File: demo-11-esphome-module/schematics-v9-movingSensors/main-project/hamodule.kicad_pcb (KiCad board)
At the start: 2 copper layers, 145.4 x 76.2 mm, 62 parts, among them J1 1017505, J2 Conn-ESP-Relays, J3 1017505, J4 Conn-Buttons, J5 Conn_01x02, J6 Conn-Esp-Sensors, J7 Conn-LedIndicators, J8 1017505, K1 G5Q-1, K2 G5Q-1, K3 G5Q-1, K4 G5Q-1, U1 ULN2003A, U2 LD1117S33TR_SOT223, U3 HCPL3700, U4 HCPL3700, U5 HCPL3700, U6 HCPL3700

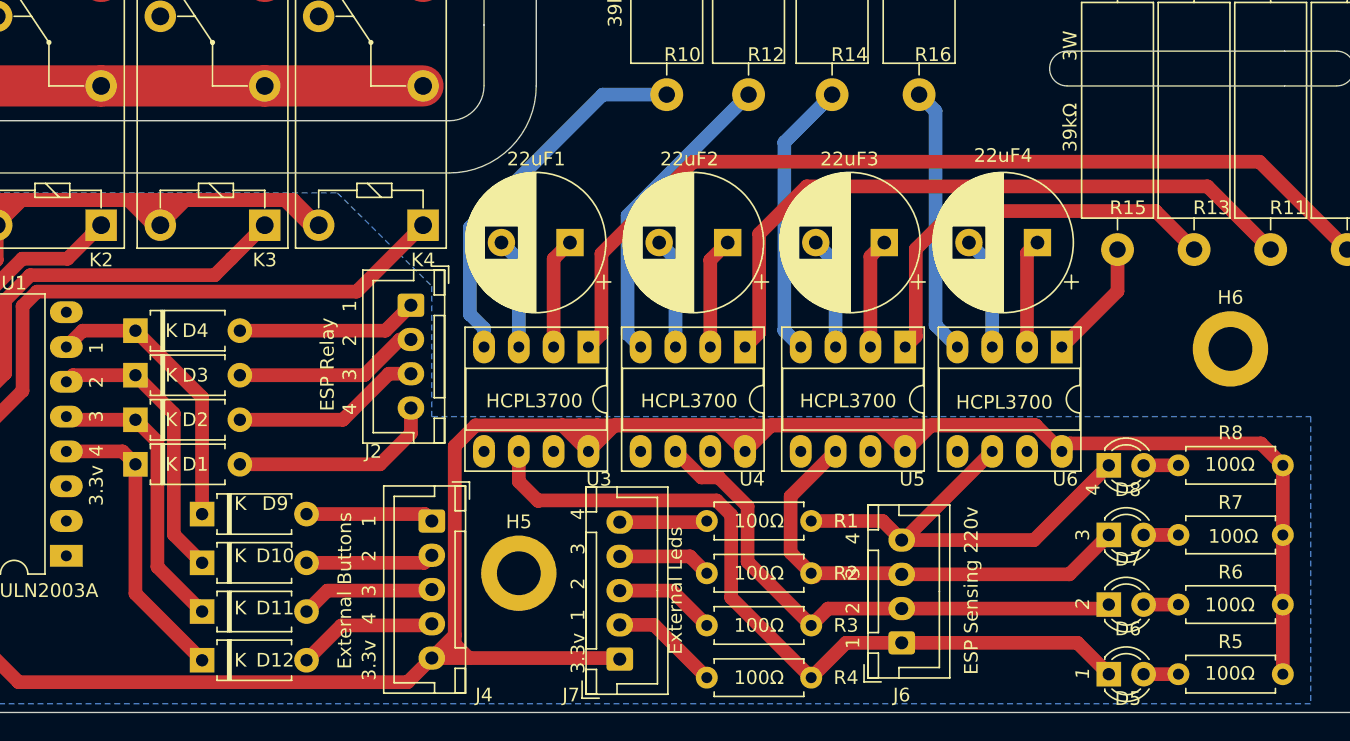
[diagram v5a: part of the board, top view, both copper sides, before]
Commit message: adding mounting holes for ESP board
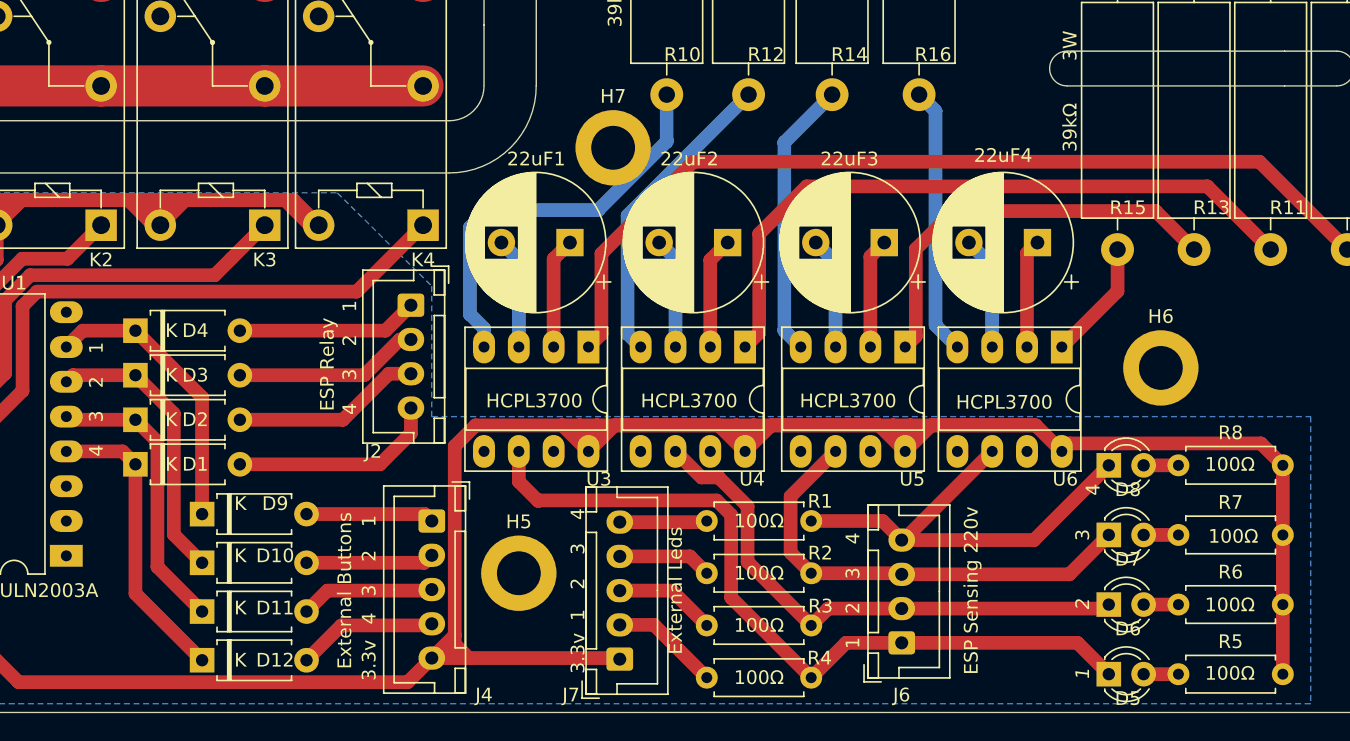
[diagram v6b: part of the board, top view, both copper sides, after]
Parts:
- added H7: MountingHole_Pad, MountingHole:MountingHole_3.2mm_M3_ISO14580_Pad, F.Cu at (109.8, 46.4)
- moved H6 5.27 mm to (149.7, 62.5)
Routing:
- net Net-(R10-Pad2): track 27.5 -> 29.5 mm
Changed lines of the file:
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@@
   (general
     (thickness 1.6)
-    (drawings 116)
-    (tracks 282)
+    (drawings 115)
+    (tracks 284)
     (zones 0)
-    (modules 62)
-    (nets 77)
+    (modules 63)
+    (nets 78)
   )
   (page A4)
   (layers
-    (0 F.Cu signal)
-    (31 B.Cu signal)
+    (0 F.Cu signal hide)
+    (31 B.Cu signal hide)
     (32 B.Adhes user hide)
     (33 F.Adhes user hide)
@@
   (net 75 "Net-(U5-Pad7)")
   (net 76 "Net-(U6-Pad7)")
+  (net 77 "Net-(H7-Pad1)")
   (net_class Default "This is the default net class."
     (clearance 0.2)
@@
     (add_net "Net-(H5-Pad1)")
     (add_net "Net-(H6-Pad1)")
+    (add_net "Net-(H7-Pad1)")
     (add_net "Net-(J3-Pad3)")
     (add_net "Net-(J3-Pad4)")
@@
     (add_net Sens4)
   )
+  (module MountingHole:MountingHole_3.2mm_M3_ISO14580_Pad (layer F.Cu)
+    (at 109.7534 46.42358)
+    (descr "Mounting Hole 3.2mm, M3, ISO14580")
+    (tags "mounting hole 3.2mm m3 iso14580")
+    (attr virtual)
+    (fp_text reference H7 (at 0 -3.75) (layer F.SilkS)
+      (effects (font (size 1 1) (thickness 0.15)))
+    )
+    (fp_text value MountingHole_Pad (at 0 3.75) (layer F.Fab)
+      (effects (font (size 1 1) (thickness 0.15)))
+    )
+    (fp_text user %R (at 0.3 0) (layer F.Fab)
+      (effects (font (size 1 1) (thickness 0.15)))
+    )
+    (fp_circle (center 0 0) (end 2.75 0) (layer Cmts.User) (width 0.15))
+    (fp_circle (center 0 0) (end 3 0) (layer F.CrtYd) (width 0.05))
+    (pad 1 thru_hole circle (at 0 0) (size 5.5 5.5) (drill 3.2) (layers *.Cu *.Mask)
+      (net 77 "Net-(H7-Pad1)"))
+  )
   (module Capacitor_THT:CP_Radial_D6.3mm_P2.50mm (layer F.Cu)
     (at 60.96 80.01 270)
@@
     (descr "Resistor, Axial_DIN0207 series, Axial, Horizontal, pin pitch=7.62mm, 0.25W = 1/4W, length*diameter=6.3*2.5mm^2, http://cdn-reichelt.de/documents/datenblatt/B400/1_4W%23YAG.pdf")
     (tags "Resistor Axial_DIN0207 series Axial Horizontal pin pitch 7.62mm 0.25W = 1/4W length 6.3mm diameter 2.5mm")
-    (fp_text reference R4 (at -2.54 0) (layer F.SilkS)
+    (fp_text reference R4 (at -0.61468 1.42494) (layer F.SilkS)
       (effects (font (size 1 1) (thickness 0.15)))
     )
@@
     (descr "Resistor, Axial_DIN0207 series, Axial, Horizontal, pin pitch=7.62mm, 0.25W = 1/4W, length*diameter=6.3*2.5mm^2, http://cdn-reichelt.de/documents/datenblatt/B400/1_4W%23YAG.pdf")
     (tags "Resistor Axial_DIN0207 series Axial Horizontal pin pitch 7.62mm 0.25W = 1/4W length 6.3mm diameter 2.5mm")
-    (fp_text reference R3 (at -2.54 0) (layer F.SilkS)
+    (fp_text reference R3 (at -0.68326 1.41224) (layer F.SilkS)
       (effects (font (size 1 1) (thickness 0.15)))
     )
@@
     (descr "Resistor, Axial_DIN0207 series, Axial, Horizontal, pin pitch=7.62mm, 0.25W = 1/4W, length*diameter=6.3*2.5mm^2, http://cdn-reichelt.de/documents/datenblatt/B400/1_4W%23YAG.pdf")
     (tags "Resistor Axial_DIN0207 series Axial Horizontal pin pitch 7.62mm 0.25W = 1/4W length 6.3mm diameter 2.5mm")
-    (fp_text reference R2 (at -2.54 0) (layer F.SilkS)
+    (fp_text reference R2 (at -0.66548 1.46812) (layer F.SilkS)
       (effects (font (size 1 1) (thickness 0.15)))
     )
@@
     (descr "Resistor, Axial_DIN0207 series, Axial, Horizontal, pin pitch=7.62mm, 0.25W = 1/4W, length*diameter=6.3*2.5mm^2, http://cdn-reichelt.de/documents/datenblatt/B400/1_4W%23YAG.pdf")
     (tags "Resistor Axial_DIN0207 series Axial Horizontal pin pitch 7.62mm 0.25W = 1/4W length 6.3mm diameter 2.5mm")
-    (fp_text reference R1 (at -2.54 0) (layer F.SilkS)
+    (fp_text reference R1 (at -0.6477 1.43764) (layer F.SilkS)
       (effects (font (size 1 1) (thickness 0.15)))
     )
@@
   )
   (module MountingHole:MountingHole_3.2mm_M3_ISO14580_Pad (layer F.Cu)
-    (at 154.8 61.1)
+    (at 149.7203 62.48908)
     (descr "Mounting Hole 3.2mm, M3, ISO14580")
     (tags "mounting hole 3.2mm m3 iso14580")
@@
     (effects (font (size 1 1) (thickness 0.15)))
   )
-  (gr_text 3.3v (at 72.044 71.07 90) (layer F.SilkS)
-    (effects (font (size 1 1) (thickness 0.15)))
-  )
   (gr_text 4 (at 91.974 31.794) (layer F.SilkS)
     (effects (font (size 1 1) (thickness 0.15) italic))
@@
   (segment (start 44.45 27.94) (end 44.45 30.48) (width 3) (layer F.Cu) (net 26))
   (segment (start 44.45 33.655) (end 44.45 27.94) (width 3) (layer F.Cu) (net 26))
-  (segment (start 99.299999 52.235999) (end 108.990998 42.545) (width 1) (layer B.Cu) (net 27))
-  (segment (start 99.299999 58.576179) (end 99.299999 52.235999) (width 1) (layer B.Cu) (net 27))
-  (segment (start 108.990998 42.545) (end 113.665 42.545) (width 1) (layer B.Cu) (net 27))
-  (segment (start 100.33 59.60618) (end 99.299999 58.576179) (width 1) (layer B.Cu) (net 27))
-  (segment (start 100.33 60.96) (end 100.33 59.60618) (width 1) (layer B.Cu) (net 27))
+  (segment (start 100.33 59.60618) (end 100.33 60.96) (width 1) (layer B.Cu) (net 27))
+  (segment (start 99.299999 58.576179) (end 100.33 59.60618) (width 1) (layer B.Cu) (net 27))
+  (segment (start 113.665 42.545) (end 113.665 45.968402) (width 1) (layer B.Cu) (net 27))
+  (segment (start 113.665 45.968402) (end 108.660682 50.97272) (width 1) (layer B.Cu) (net 27))
+  (segment (start 108.660682 50.97272) (end 100.563278 50.97272) (width 1) (layer B.Cu) (net 27))
+  (segment (start 100.563278 50.97272) (end 99.299999 52.235999) (width 1) (layer B.Cu) (net 27))
+  (segment (start 99.299999 52.235999) (end 99.299999 58.576179) (width 1) (layer B.Cu) (net 27))
   (segment (start 140.469 75.05) (end 145.923 69.596) (width 1) (layer F.Cu) (net 28))
   (segment (start 130.81 75.05) (end 140.469 75.05) (width 1) (layer F.Cu) (net 28))

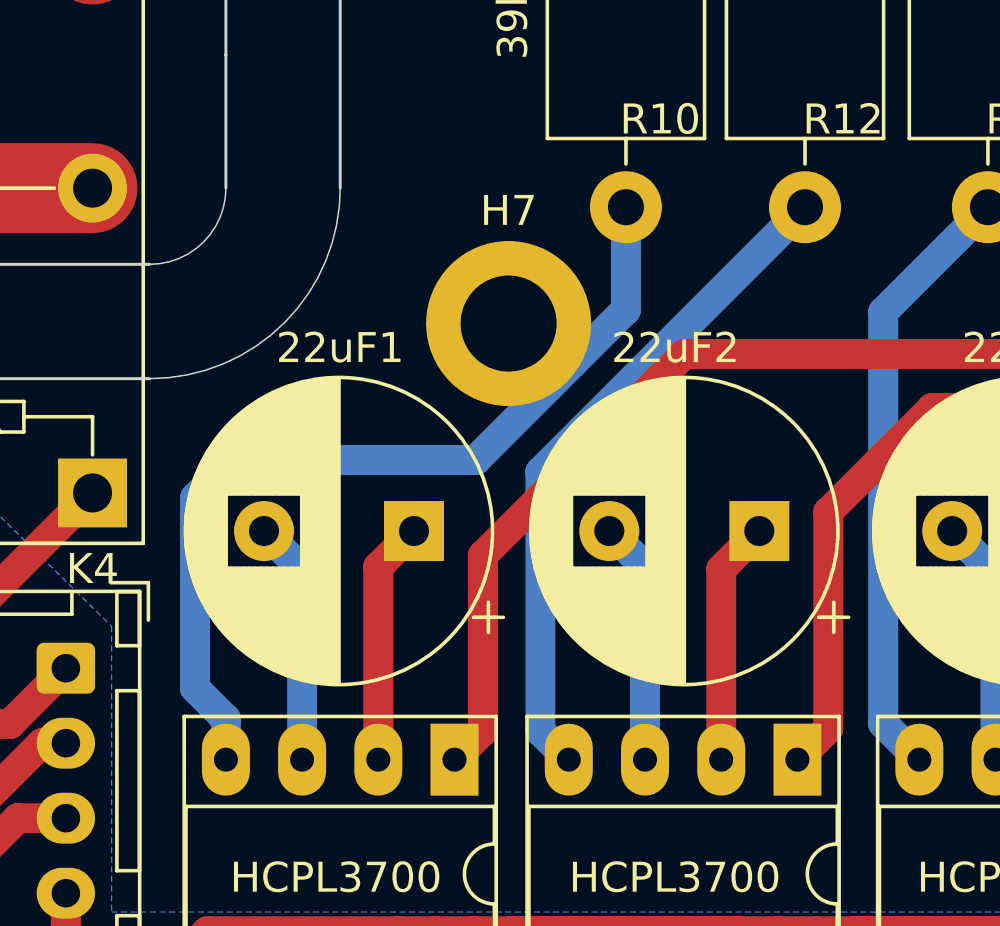
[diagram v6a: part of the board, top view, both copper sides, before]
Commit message: mounting holes + text correction + ...
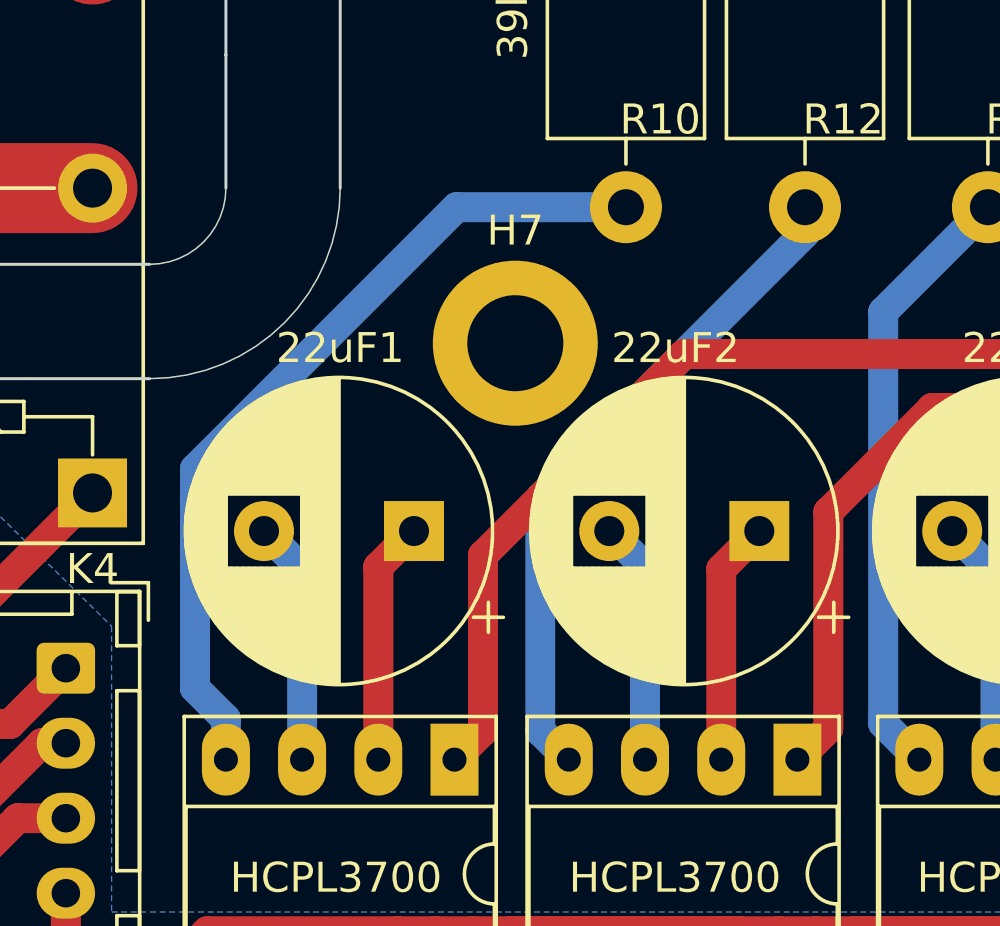
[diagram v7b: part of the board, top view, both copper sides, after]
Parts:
- moved H7 0.69 mm to (110.0, 47.1)
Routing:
- net Net-(R10-Pad2): track 29.5 -> 28.1 mm
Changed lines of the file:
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@@
     (thickness 1.6)
     (drawings 115)
-    (tracks 284)
+    (tracks 283)
     (zones 0)
     (modules 63)
@@
   (page A4)
   (layers
-    (0 F.Cu signal hide)
+    (0 F.Cu signal)
     (31 B.Cu signal hide)
     (32 B.Adhes user hide)
@@
   )
   (module MountingHole:MountingHole_3.2mm_M3_ISO14580_Pad (layer F.Cu)
-    (at 109.7534 46.42358)
+    (at 109.97692 47.0789)
     (descr "Mounting Hole 3.2mm, M3, ISO14580")
     (tags "mounting hole 3.2mm m3 iso14580")
@@
   (segment (start 100.33 59.60618) (end 100.33 60.96) (width 1) (layer B.Cu) (net 27))
   (segment (start 99.299999 58.576179) (end 100.33 59.60618) (width 1) (layer B.Cu) (net 27))
-  (segment (start 113.665 42.545) (end 113.665 45.968402) (width 1) (layer B.Cu) (net 27))
-  (segment (start 113.665 45.968402) (end 108.660682 50.97272) (width 1) (layer B.Cu) (net 27))
-  (segment (start 108.660682 50.97272) (end 100.563278 50.97272) (width 1) (layer B.Cu) (net 27))
-  (segment (start 100.563278 50.97272) (end 99.299999 52.235999) (width 1) (layer B.Cu) (net 27))
-  (segment (start 99.299999 52.235999) (end 99.299999 58.576179) (width 1) (layer B.Cu) (net 27))
+  (segment (start 99.299999 51.264549) (end 99.299999 58.576179) (width 1) (layer B.Cu) (net 27))
+  (segment (start 108.019548 42.545) (end 99.299999 51.264549) (width 1) (layer B.Cu) (net 27))
+  (segment (start 113.665 42.545) (end 108.019548 42.545) (width 1) (layer B.Cu) (net 27))
   (segment (start 140.469 75.05) (end 145.923 69.596) (width 1) (layer F.Cu) (net 28))
   (segment (start 130.81 75.05) (end 140.469 75.05) (width 1) (layer F.Cu) (net 28))
@@
   (segment (start 157.734 53.848) (end 153.125989 49.239989) (width 1) (layer F.Cu) (net 47))
   (segment (start 110.809999 60.009999) (end 111.76 60.96) (width 1) (layer B.Cu) (net 48))
-  (segment (start 110.809999 51.369001) (end 110.809999 60.009999) (width 1) (layer B.Cu) (net 48))
-  (segment (start 119.634 42.545) (end 110.809999 51.369001) (width 1) (layer B.Cu) (net 48))
+  (segment (start 110.809999 52.239823) (end 110.809999 60.009999) (width 1) (layer B.Cu) (net 48))
+  (segment (start 119.634 43.415822) (end 110.809999 52.239823) (width 1) (layer B.Cu) (net 48))
+  (segment (start 119.634 42.545) (end 119.634 43.415822) (width 1) (layer B.Cu) (net 48))
   (segment (start 134.611999 51.039999) (end 131.840001 53.811997) (width 1) (layer F.Cu) (net 49))
   (segment (start 149.337999 51.039999) (end 134.611999 51.039999) (width 1) (layer F.Cu) (net 49))

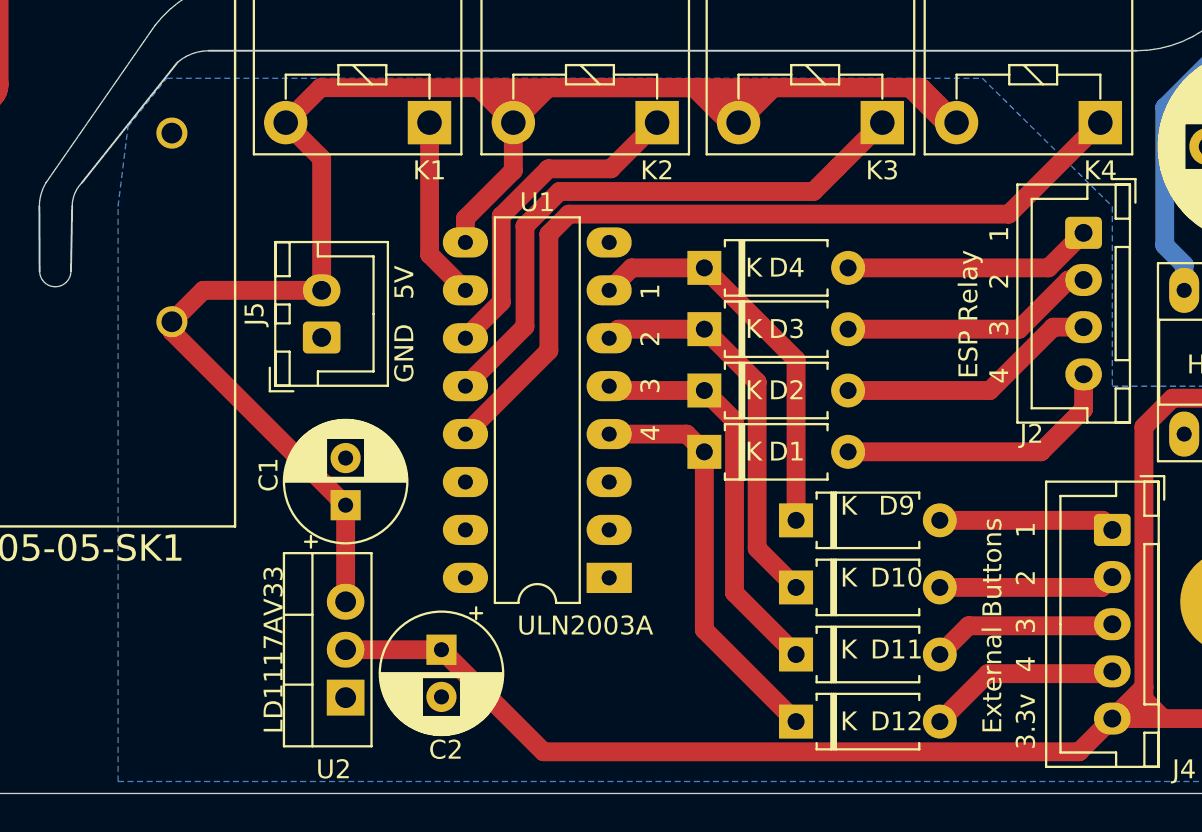
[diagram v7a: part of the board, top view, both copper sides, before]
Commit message: adding pins to mesure current
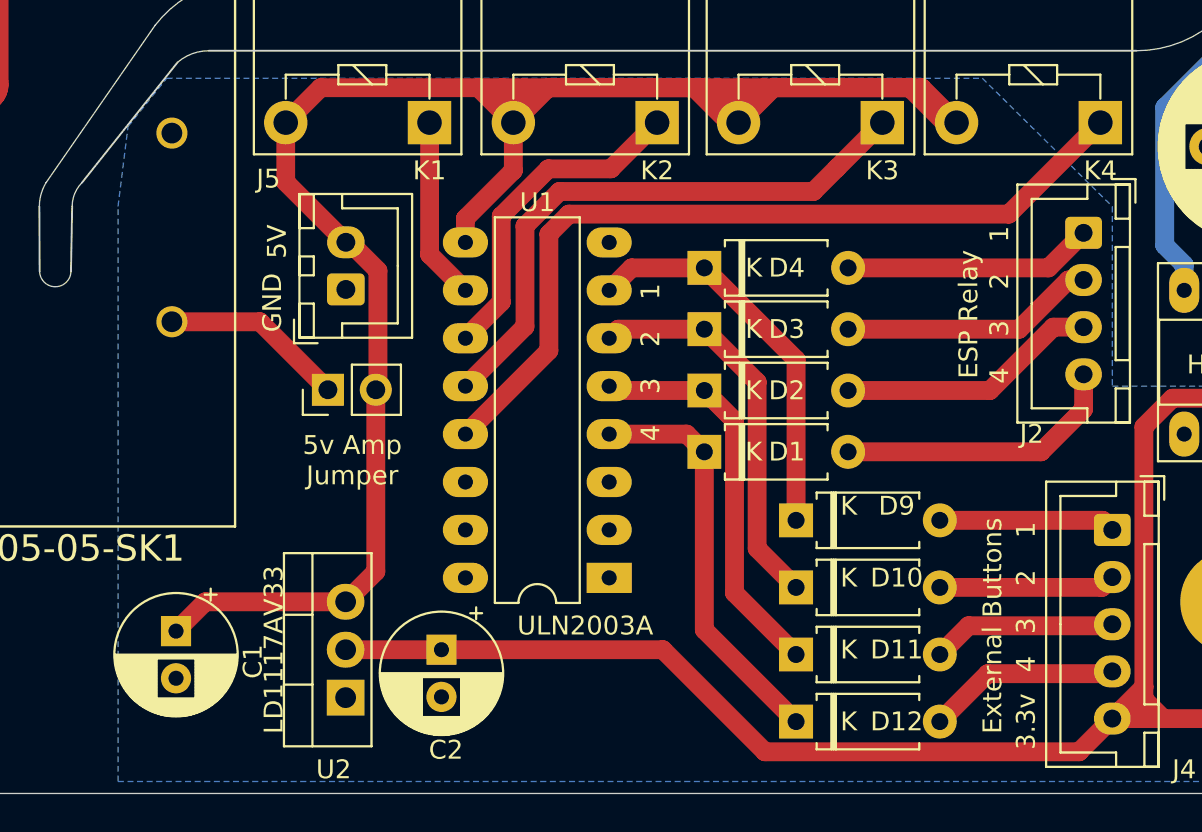
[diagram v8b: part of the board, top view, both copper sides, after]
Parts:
- added Jumper-5vAmpMeter: Conn_01x02_Male, Connector_PinHeader_2.54mm:PinHeader_1x02_P2.54mm_Vertical, F.Cu at (54.9, 66.2)
- moved C1 11.2 mm to (46.9, 79.0), turned to 270 degrees
- moved J5 2.85 mm to (55.9, 60.9)
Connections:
- RA05-05-SK1 pad 7: 5V+ -> Net-(J9-Pad1)
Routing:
- net Net-(J9-Pad1): track 0.00 -> 9.76 mm
- net 5V+: track 121.1 -> 122.0 mm
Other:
- board text added: "5v Amp Jumper"
